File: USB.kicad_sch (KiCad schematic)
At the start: 35 parts, among them J1 JST_PH_01x06, J2 Conn_01x02, J3 Conn_01x02, J4 Conn_01x02, J5 USB_A, J6 JST_PH_01x06, U1 TPS25751D, U2 CAT24C256

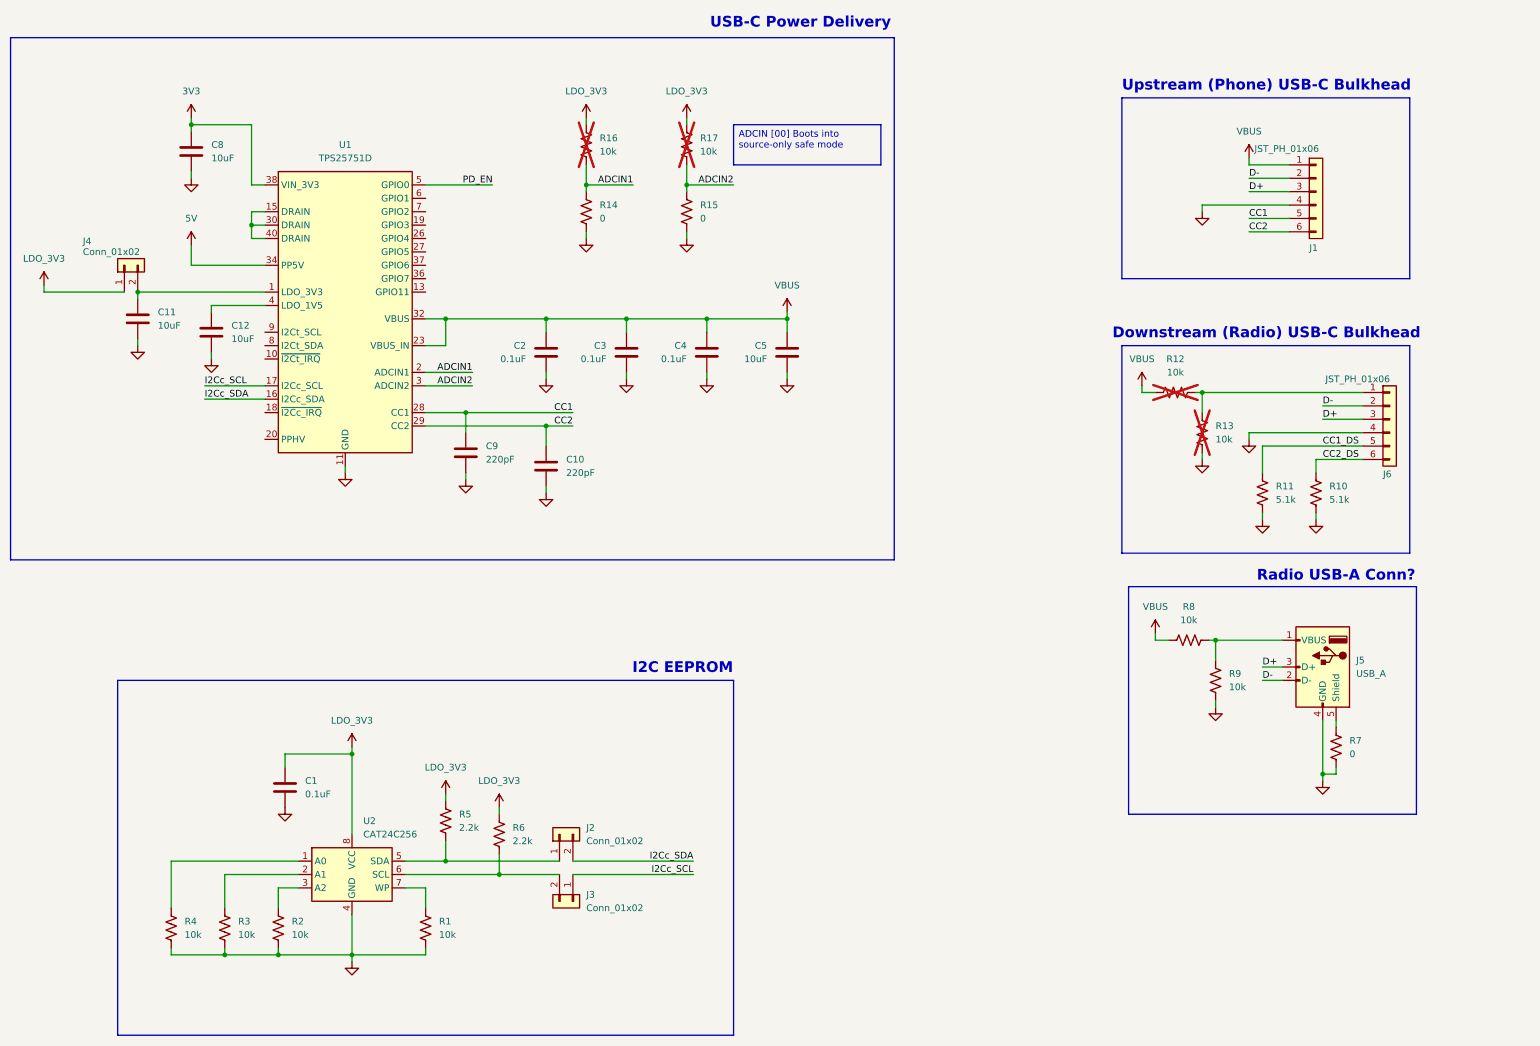
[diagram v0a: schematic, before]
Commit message: add power supplies
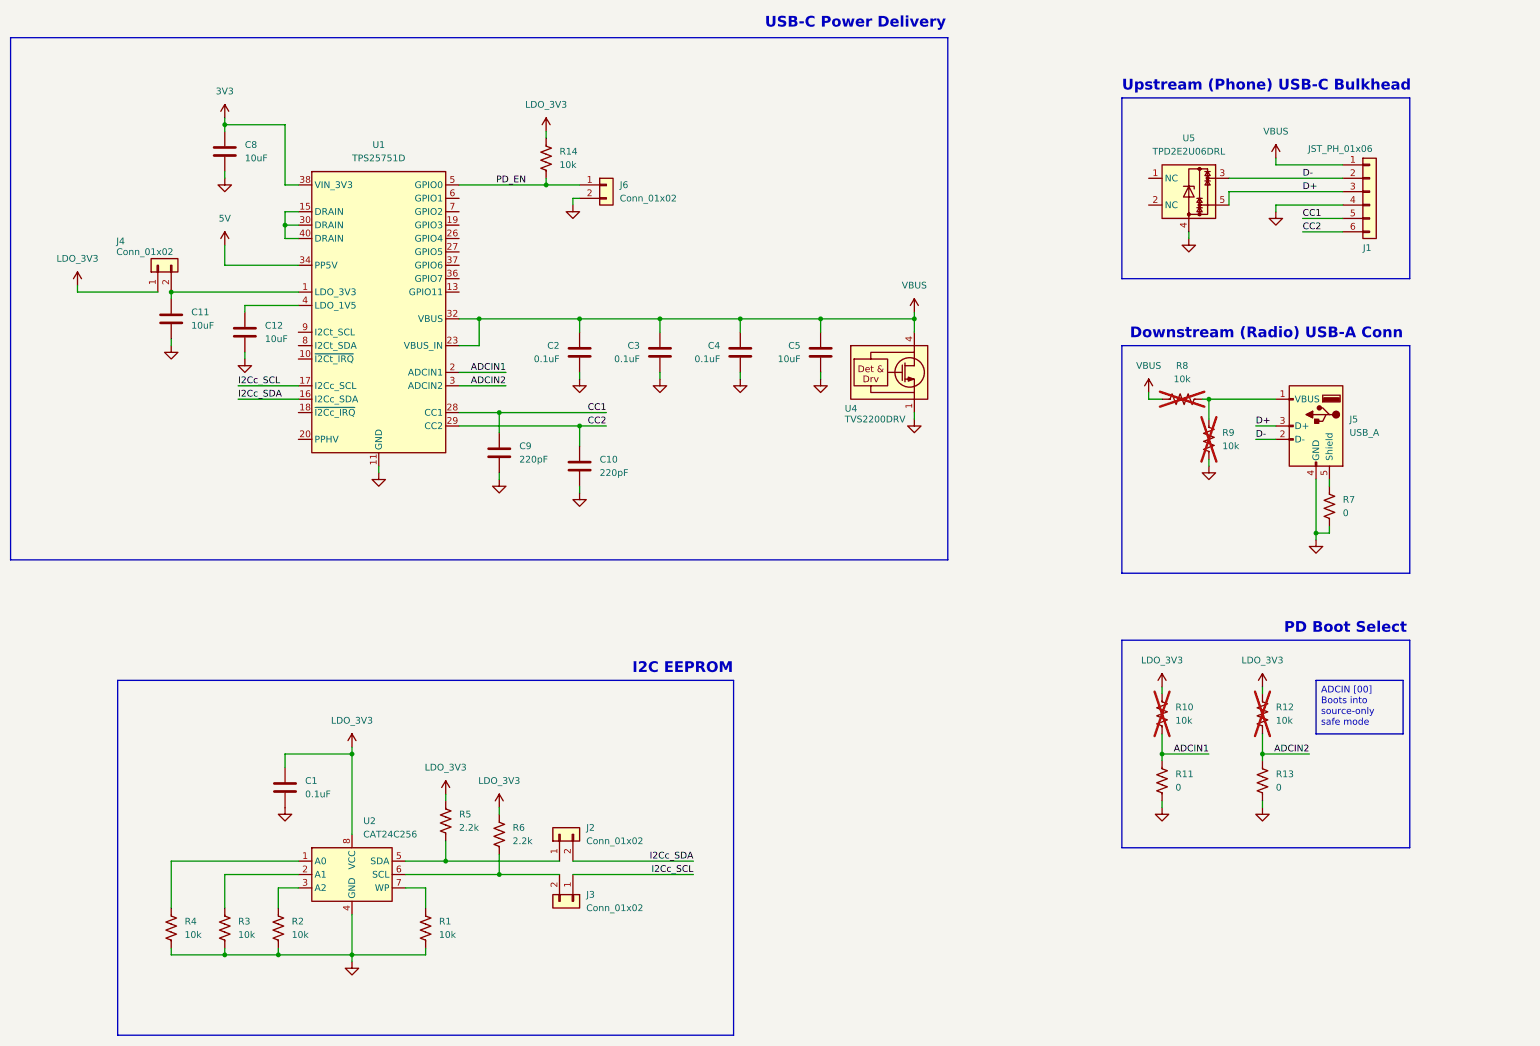
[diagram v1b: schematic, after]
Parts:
- removed J6: JST_PH_01x06, symbol Cave_Radio_PDB:JST_PH_01x06
- removed R10, R11: 5.1k, symbol Cave_Radio_PDB:5.1k
- removed R13, R16, R17: 10k, symbol Cave_Radio_PDB:10k
- removed R14, R15: 0, symbol Cave_Radio_PDB:0
- added J6: Conn_01x02, symbol Cave_Radio_PDB:Conn_01x02
- added R10, R14: 10k, symbol Cave_Radio_PDB:10k
- added R11, R13: 0, symbol Cave_Radio_PDB:0
- added U4: TVS2200DRV, Package_SON:WSON-6-1EP_2x2mm_P0.65mm_EP1x1.6mm, symbol Cave_Radio_PDB:TVS2200DRV
- added U5: TPD2E2U06DRL, Package_TO_SOT_SMD:SOT-553, symbol Cave_Radio_PDB:TPD2E2U06DRL
- R8, R9: now not fitted
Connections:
- net ADCIN1: now also R10.2, R11.1
- net ADCIN2: now also R12.2, R13.1
- net D+: now also U5.5
- net D-: now also U5.3
- net GND: now also J6.2 (Pin_2), R11.2, R13.2, U4.1 (GND), U4.2 (GND), U4.3 (GND), U4.7 (GND), U5.4
- net LDO_3V3: now also R12.1, R10.1, R14.1
- net PD_EN: now also J6.1 (Pin_1), R14.2
- net VBUS: now also U4.4 (IN), U4.5 (IN), U4.6 (IN); no longer R12.1
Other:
- note added: "Downstream (Radio) USB-A Conn"
- note added: "PD Boot Select"
- note removed: "Downstream (Radio) USB-C Bulkhead"
- note removed: "Radio USB-A Conn?"
- moved on the sheet: C10, C11, C12, C2, C3, C4, C5, C8, C9, J1, J4, J5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

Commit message: start efuse and rough layout
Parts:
- C1, C10, C11, C12, C2, C3, C4, C5, C8, C9: footprint (none) -> Cave_Radio_PDB:C_0402_1005Metric
- J1: footprint (none) -> Cave_Radio_PDB:CONN6_S6B-PH_JST
- J2, J3, J4, J6: footprint (none) -> Cave_Radio_PDB:CONN_TSW-102-S_SAI
- J5: footprint (none) -> Cave_Radio_PDB:CINCH_SS-52100-001
- R1, R10, R11, R12, R13, R14, R2, R3, R4, R5, R6, R7, R8, R9: footprint (none) -> Cave_Radio_PDB:R_0402_1005Metric
- U2: footprint (none) -> Cave_Radio_PDB:SOIC-8_5.3x5.3mm_P1.27mm
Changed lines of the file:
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@@
 			)
 		)
-		(property "Footprint" ""
+		(property "Footprint" "Cave_Radio_PDB:C_0402_1005Metric"
 			(at 223.8248 132.08 0)
 			(effects
@@
 			)
 		)
-		(property "Footprint" ""
+		(property "Footprint" "Cave_Radio_PDB:C_0402_1005Metric"
 			(at 143.2052 93.98 0)
 			(effects
@@
 			)
 		)
-		(property "Footprint" ""
+		(property "Footprint" "Cave_Radio_PDB:R_0402_1005Metric"
 			(at 133.096 237.744 90)
 			(effects
@@
 			)
 		)
-		(property "Footprint" ""
+		(property "Footprint" "Cave_Radio_PDB:R_0402_1005Metric"
 			(at 340.106 197.104 90)
 			(effects
@@
 			)
 		)
-		(property "Footprint" ""
+		(property "Footprint" "Cave_Radio_PDB:R_0402_1005Metric"
 			(at 321.056 197.104 90)
 			(effects
@@
 			)
 		)
-		(property "Footprint" ""
+		(property "Footprint" "Cave_Radio_PDB:CONN_TSW-102-S_SAI"
 			(at 214.63 96.52 0)
 			(effects
@@
 			)
 		)
-		(property "Footprint" ""
+		(property "Footprint" "Cave_Radio_PDB:CONN_TSW-102-S_SAI"
 			(at 129.54 111.76 0)
 			(effects
@@
 			)
 		)
-		(property "Footprint" ""
+		(property "Footprint" "Cave_Radio_PDB:R_0402_1005Metric"
 			(at 324.104 136.144 90)
 			(effects
@@
 			)
 		)
-		(property "Footprint" ""
+		(property "Footprint" "Cave_Radio_PDB:CONN_TSW-102-S_SAI"
 			(at 208.28 232.41 0)
 			(effects
@@
 			)
 		)
-		(property "Footprint" ""
+		(property "Footprint" "Cave_Radio_PDB:C_0402_1005Metric"
 			(at 254.3048 132.08 0)
 			(effects
@@
 			)
 		)
-		(property "Footprint" ""
+		(property "Footprint" "Cave_Radio_PDB:C_0402_1005Metric"
 			(at 239.0648 132.08 0)
 			(effects
@@
 			)
 		)
-		(property "Footprint" ""
+		(property "Footprint" "Cave_Radio_PDB:R_0402_1005Metric"
 			(at 327.914 144.526 90)
 			(effects
@@
 			)
 		)
-		(property "Footprint" ""
+		(property "Footprint" "Cave_Radio_PDB:R_0402_1005Metric"
 			(at 153.416 237.744 90)
 			(effects
@@
 			)
 		)
-		(property "Footprint" ""
+		(property "Footprint" "Cave_Radio_PDB:R_0402_1005Metric"
 			(at 340.106 209.804 90)
 			(effects
@@
 			)
 		)
-		(property "Footprint" ""
+		(property "Footprint" "Cave_Radio_PDB:SOIC-8_5.3x5.3mm_P1.27mm"
 			(at 166.37 227.33 0)
 			(effects
@@
 			)
 		)
-		(property "Footprint" ""
+		(property "Footprint" "Cave_Radio_PDB:R_0402_1005Metric"
 			(at 352.806 157.734 90)
 			(effects
@@
 			)
 		)
-		(property "Footprint" ""
+		(property "Footprint" "Cave_Radio_PDB:CONN_TSW-102-S_SAI"
 			(at 205.74 219.71 0)
 			(effects
@@
 			)
 		)
-		(property "Footprint" ""
+		(property "Footprint" "Cave_Radio_PDB:CINCH_SS-52100-001"
 			(at 345.44 143.51 0)
 			(effects
@@
 			)
 		)
-		(property "Footprint" ""
+		(property "Footprint" "Cave_Radio_PDB:R_0402_1005Metric"
 			(at 185.166 217.424 90)
 			(effects
@@
 			)
 		)
-		(property "Footprint" ""
+		(property "Footprint" "Cave_Radio_PDB:R_0402_1005Metric"
 			(at 195.326 219.964 90)
 			(effects
@@
 			)
 		)
-		(property "Footprint" ""
+		(property "Footprint" "Cave_Radio_PDB:C_0402_1005Metric"
 			(at 208.5848 132.08 0)
 			(effects
@@
 			)
 		)
-		(property "Footprint" ""
+		(property "Footprint" "Cave_Radio_PDB:C_0402_1005Metric"
 			(at 195.2752 151.13 0)
 			(effects
@@
 			)
 		)
-		(property "Footprint" ""
+		(property "Footprint" "Cave_Radio_PDB:R_0402_1005Metric"
 			(at 321.056 209.804 90)
 			(effects
@@
 			)
 		)
-		(property "Footprint" ""
+		(property "Footprint" "Cave_Radio_PDB:CONN6_S6B-PH_JST"
 			(at 359.41 97.79 0)
 			(effects
@@
 			)
 		)
-		(property "Footprint" ""
+		(property "Footprint" "Cave_Radio_PDB:C_0402_1005Metric"
 			(at 147.0152 128.27 0)
 			(effects
@@
 			)
 		)
-		(property "Footprint" ""
+		(property "Footprint" "Cave_Radio_PDB:R_0402_1005Metric"
 			(at 143.256 237.744 90)
 			(effects
@@
 			)
 		)
-		(property "Footprint" ""
+		(property "Footprint" "Cave_Radio_PDB:R_0402_1005Metric"
 			(at 204.216 91.694 90)
 			(effects
@@
 			)
 		)
-		(property "Footprint" ""
+		(property "Footprint" "Cave_Radio_PDB:C_0402_1005Metric"
 			(at 154.6352 214.63 0)
 			(effects
@@
 			)
 		)
-		(property "Footprint" ""
+		(property "Footprint" "Cave_Radio_PDB:C_0402_1005Metric"
 			(at 210.5152 153.67 0)
 			(effects
@@
 			)
 		)
-		(property "Footprint" ""
+		(property "Footprint" "Cave_Radio_PDB:C_0402_1005Metric"
 			(at 133.0452 125.73 0)
 			(effects
@@
 			)
 		)
-		(property "Footprint" ""
+		(property "Footprint" "Cave_Radio_PDB:R_0402_1005Metric"
 			(at 181.356 237.744 90)
 			(effects

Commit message: finish efuse schematic, update connectors
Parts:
- removed C10, C9: 220pF, Cave_Radio_PDB:C_0402_1005Metric, symbol Cave_Radio_PDB:220pF
- removed C4: 0.1uF, Cave_Radio_PDB:C_0402_1005Metric, symbol Cave_Radio_PDB:0.1uF
- removed J1: JST_PH_01x06, Cave_Radio_PDB:CONN6_S6B-PH_JST, symbol Cave_Radio_PDB:JST_PH_01x06
- removed J5: USB_A, Cave_Radio_PDB:CINCH_SS-52100-001, symbol Cave_Radio_PDB:USB_A
- removed R7: 0, Cave_Radio_PDB:R_0402_1005Metric, symbol Cave_Radio_PDB:0
- removed R8, R9: 10k, Cave_Radio_PDB:R_0402_1005Metric, symbol Cave_Radio_PDB:10k
- added C10, C9: 1nF, symbol Cave_Radio_PDB:1nF
- added C4: 10uF, Cave_Radio_PDB:C_0402_1005Metric, symbol Cave_Radio_PDB:10uF
- added J5: Conn_01x03, symbol Cave_Radio_PDB:Conn_01x03
- added J9: USB4110GFA, USB4110GFA:GCT_USB4110GFA, symbol Cave_Radio_PDB:USB4110GFA
- added R24, R25, R26: 0, Cave_Radio_PDB:R_0402_1005Metric, symbol Cave_Radio_PDB:0
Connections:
- net CC1: now also C9.1, J9.A5 (CC1)
- net CC2: now also C10.1, J9.B5 (CC2)
- net D+: now also U5.3, J5.1 (Pin_1), J9.A6 (DP1), J9.B6 (DP2); no longer U5.5
- net D-: now also U5.5, J5.2 (Pin_2), J9.A7 (DN1), J9.B7 (DN2); no longer U5.3
- net GND: now also C10.2, C4.2, C9.2, J5.3 (Pin_3), J9.A1/B12 (GND), J9.B1/A12 (GND), J9.S1 (GND), J9.S2 (GND), J9.S3 (GND), J9.S4 (GND)
- net I2Cc_SCL: now also R26.2
- net I2Cc_SDA: now also R25.2
- net LDO_3V3: now also R24.1
- net VBUS: now also C4.1, J9.A4/B9 (VBUS), J9.B4/A9 (VBUS)
- net at C11.1, J4.2 (Pin_2), U1.1 (LDO_3V3): now also R24.2
- net at J3.2 (Pin_2), R6.2, U2.6 (SCL): now also R26.1
- net at J2.1 (Pin_1), R5.2, U2.5 (SDA): now also R25.1
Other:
- note added: "Radio Data Conn"
- note added: "USB-C Conn"
- note removed: "Downstream (Radio) USB-A Conn"
- note removed: "Upstream (Phone) USB-C Bulkhead"
- moved on the sheet: C5, J4, U5

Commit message: Update footprints
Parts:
- C10, C9: footprint (none) -> Cave_Radio_PDB:C_0402_1005Metric
- C11, C12, C4, C5, C8: footprint Cave_Radio_PDB:C_0402_1005Metric -> Cave_Radio_PDB:R_0603_1608Metric
- J5: footprint (none) -> Cave_Radio_PDB:CONN_TSW-103-S_SAI
- J9: footprint USB4110GFA:GCT_USB4110GFA -> Cave_Radio_PDB:GCT_USB4110GFA
- U1: footprint Package_DFN_QFN:Texas_REF0038A_WQFN-38-2EP_6x4mm_P0.4 -> Cave_Radio_PDB:Texas_REF0038A_WQFN-38-2EP_6x4mm_P0.4
- U4: footprint Package_SON:WSON-6-1EP_2x2mm_P0.65mm_EP1x1.6mm -> Cave_Radio_PDB:WSON-6-1EP_2x2mm_P0.65mm_EP1x1.6mm_ThermalVias
- U5: footprint Package_TO_SOT_SMD:SOT-553 -> Cave_Radio_PDB:SOT-553
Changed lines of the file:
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@@
 			)
 		)
-		(property "Footprint" ""
+		(property "Footprint" "Cave_Radio_PDB:C_0402_1005Metric"
 			(at 210.5152 153.67 0)
 			(effects
@@
 			)
 		)
-		(property "Footprint" "Cave_Radio_PDB:C_0402_1005Metric"
+		(property "Footprint" "Cave_Radio_PDB:R_0603_1608Metric"
 			(at 143.2052 93.98 0)
 			(effects
@@
 			)
 		)
-		(property "Footprint" "Package_SON:WSON-6-1EP_2x2mm_P0.65mm_EP1x1.6mm"
+		(property "Footprint" "Cave_Radio_PDB:WSON-6-1EP_2x2mm_P0.65mm_EP1x1.6mm_ThermalVias"
 			(at 278.13 140.97 0)
 			(effects
@@
 			)
 		)
-		(property "Footprint" ""
+		(property "Footprint" "Cave_Radio_PDB:C_0402_1005Metric"
 			(at 195.2752 151.13 0)
 			(effects
@@
 			)
 		)
-		(property "Footprint" ""
+		(property "Footprint" "Cave_Radio_PDB:CONN_TSW-103-S_SAI"
 			(at 342.9 146.05 0)
 			(effects
@@
 			)
 		)
-		(property "Footprint" "Cave_Radio_PDB:C_0402_1005Metric"
+		(property "Footprint" "Cave_Radio_PDB:R_0603_1608Metric"
 			(at 254.3048 132.08 0)
 			(effects
@@
 			)
 		)
-		(property "Footprint" "Cave_Radio_PDB:C_0402_1005Metric"
+		(property "Footprint" "Cave_Radio_PDB:R_0603_1608Metric"
 			(at 239.0648 132.08 0)
 			(effects
@@
 			)
 		)
-		(property "Footprint" "USB4110GFA:GCT_USB4110GFA"
+		(property "Footprint" "Cave_Radio_PDB:GCT_USB4110GFA"
 			(at 360.426 68.072 0)
 			(effects
@@
 			)
 		)
-		(property "Footprint" "Cave_Radio_PDB:C_0402_1005Metric"
+		(property "Footprint" "Cave_Radio_PDB:R_0603_1608Metric"
 			(at 147.0152 128.27 0)
 			(effects
@@
 			)
 		)
-		(property "Footprint" "Package_DFN_QFN:Texas_REF0038A_WQFN-38-2EP_6x4mm_P0.4"
+		(property "Footprint" "Cave_Radio_PDB:Texas_REF0038A_WQFN-38-2EP_6x4mm_P0.4"
 			(at 175.26 175.26 0)
 			(effects
@@
 			)
 		)
-		(property "Footprint" "Package_TO_SOT_SMD:SOT-553"
+		(property "Footprint" "Cave_Radio_PDB:SOT-553"
 			(at 328.93 97.79 0)
 			(effects
@@
 			)
 		)
-		(property "Footprint" "Cave_Radio_PDB:C_0402_1005Metric"
+		(property "Footprint" "Cave_Radio_PDB:R_0603_1608Metric"
 			(at 133.0452 125.73 0)
 			(effects

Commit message: start layout
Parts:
- removed C5, C8: 10uF, Cave_Radio_PDB:R_0603_1608Metric, symbol Cave_Radio_PDB:10uF
- removed J2, J3, J4: Conn_01x02, Cave_Radio_PDB:CONN_TSW-102-S_SAI, symbol Cave_Radio_PDB:Conn_01x02
- removed U2: CAT24C256, Cave_Radio_PDB:SOIC-8_5.3x5.3mm_P1.27mm, symbol Memory_EEPROM:CAT24C256
- added TP1, TP2, TP3: TP_01, Cave_Radio_PDB:CONN_TP, symbol Cave_Radio_PDB:TP_1
- added U2: CAT24C256, Cave_Radio_PDB:UDFN8_2X3_ONS, symbol Cave_Radio_PDB:CAT24C256
- R24, R25, R26: now fitted
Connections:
- net GND: now also R14.2, U2.4 (GND), U2.9 (PAD); no longer J6.2 (Pin_2)
- net LDO_3V3: now also C11.1, J6.2 (Pin_2), R24.2, U1.1 (LDO_3V3); no longer C1.1, R14.1, R24.1, R5.1, R6.1
- net PD_EN: now also R14.1; no longer R14.2
- net at R4.1: now also U2.1 (A0)
- net at R26.1, R6.2: now also TP2.1 (Pin_1), U2.6 (SCL)
- net at R2.1: now also U2.3 (A2)
- net at R3.1: now also U2.2 (A1)
- net at R25.1, R5.2: now also TP3.1 (Pin_1), U2.5 (SDA)
- net at R1.1: now also U2.7 (WP)
- new net 3V3_EEPROM: C1.1, R24.1, R5.1, R6.1, TP1.1 (Pin_1), U2.8 (VCC)
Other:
- moved on the sheet: C10, C11, C12, C2, C3, C4, C9, J6, R14, U1, U4

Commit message: initial layout
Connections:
- net D+: now also J5.2 (Pin_2); no longer J5.1 (Pin_1)
- net D-: now also J5.3 (Pin_3); no longer J5.2 (Pin_2)
- net GND: now also J5.1 (Pin_1); no longer J5.3 (Pin_3)
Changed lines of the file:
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@@
 	)
 	(label "D-"
-		(at 334.01 146.05 0)
+		(at 334.01 143.51 0)
 		(effects
 			(font
@@
 	)
 	(label "D+"
-		(at 334.01 143.51 0)
+		(at 334.01 146.05 0)
 		(effects
 			(font
@@
 		(lib_id "Cave_Radio_PDB:Conn_01x03")
 		(at 342.9 146.05 0)
-		(unit 1)
-		(exclude_from_sim no)
-		(in_bom yes)
-		(on_board yes)
-		(dnp no)
-		(fields_autoplaced yes)
+		(mirror x)
+		(unit 1)
+		(exclude_from_sim no)
+		(in_bom yes)
+		(on_board yes)
+		(dnp no)
 		(property "Reference" "J5"
-			(at 345.44 144.7799 0)
+			(at 345.44 147.3201 0)
 			(effects
 				(font
@@
 		)
 		(property "Value" "Conn_01x03"
-			(at 345.44 147.3199 0)
-			(effects
-				(font
+			(at 345.44 144.7801 0)
+			(effects
+				(font

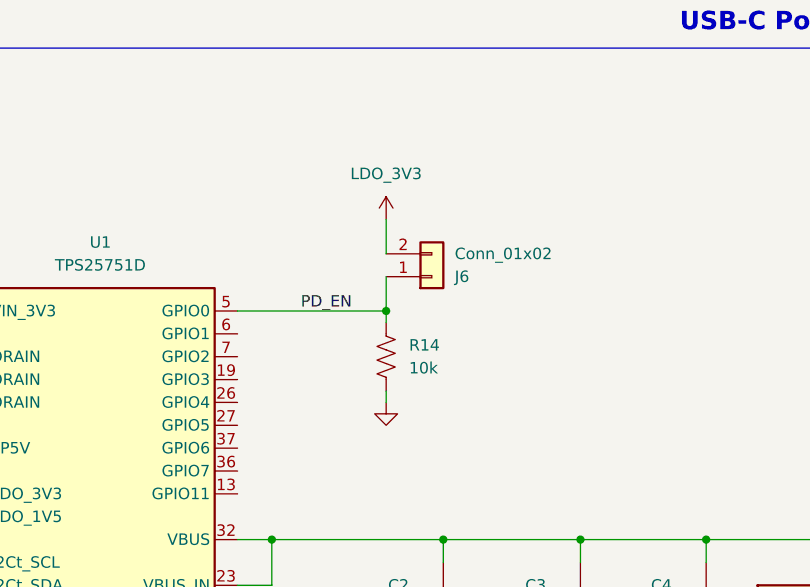
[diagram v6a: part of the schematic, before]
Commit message: remove efuse, add led connectors
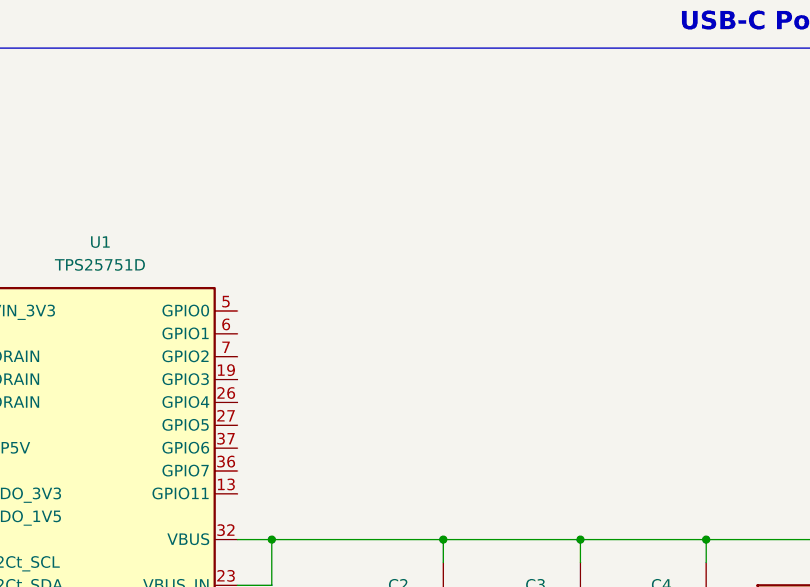
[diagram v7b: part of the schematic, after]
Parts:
- removed J6: Conn_01x02, Cave_Radio_PDB:CONN_TSW-102-S_SAI, symbol Cave_Radio_PDB:Conn_01x02
- removed R14: 10k, Cave_Radio_PDB:R_0402_1005Metric, symbol Cave_Radio_PDB:10k
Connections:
- net PD_EN: no longer names the net of U1.5 (GPIO0)
